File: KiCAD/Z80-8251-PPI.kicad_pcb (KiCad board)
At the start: 2 copper layers, 99.7 x 74.9 mm, 37 parts, among them J1 SBC8080 BUS, J2 ADDR_JP, J3 IR JP, J4 232C-CON, J5 CON-A, J6 CON-B, J7 SERIAL JP, J8 SP JP, Q1 2SC1815, U1 74LS139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

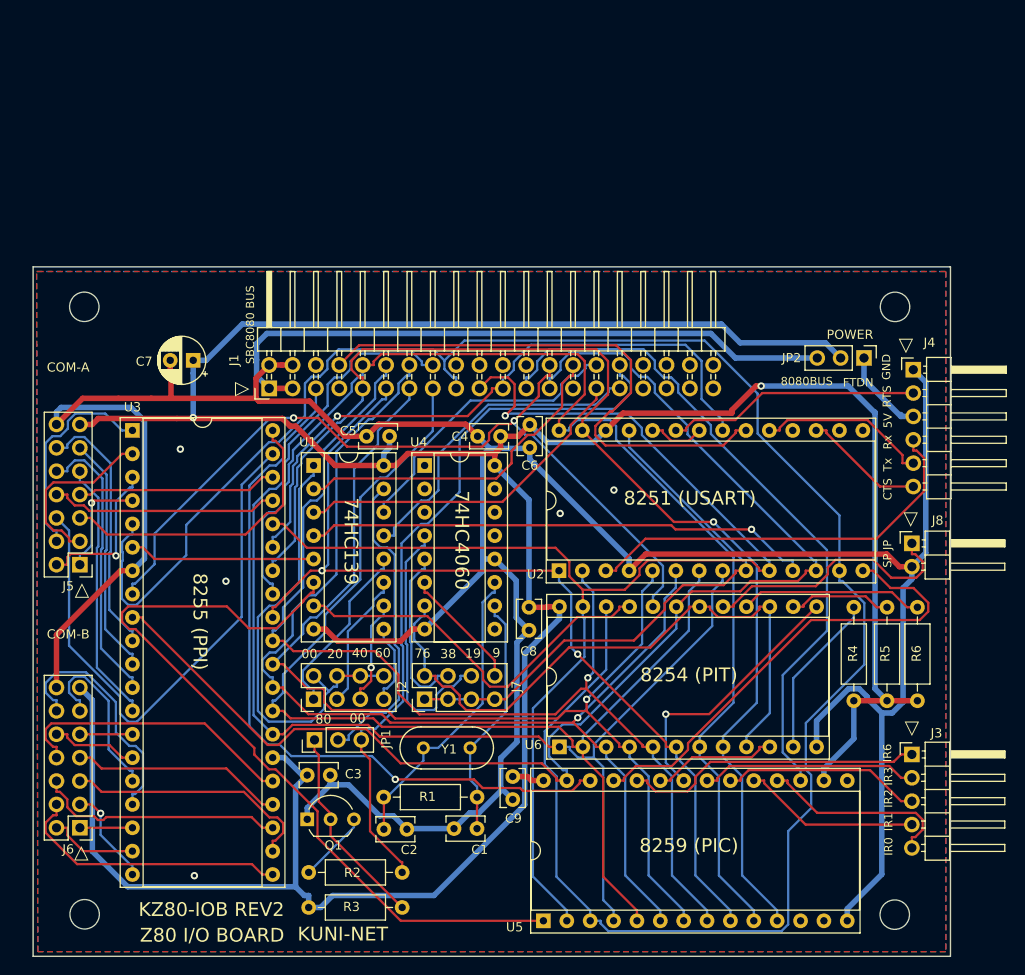
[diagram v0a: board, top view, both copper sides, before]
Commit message: ロジックICで割り込みコントローラ構成を検討 ドラフト版
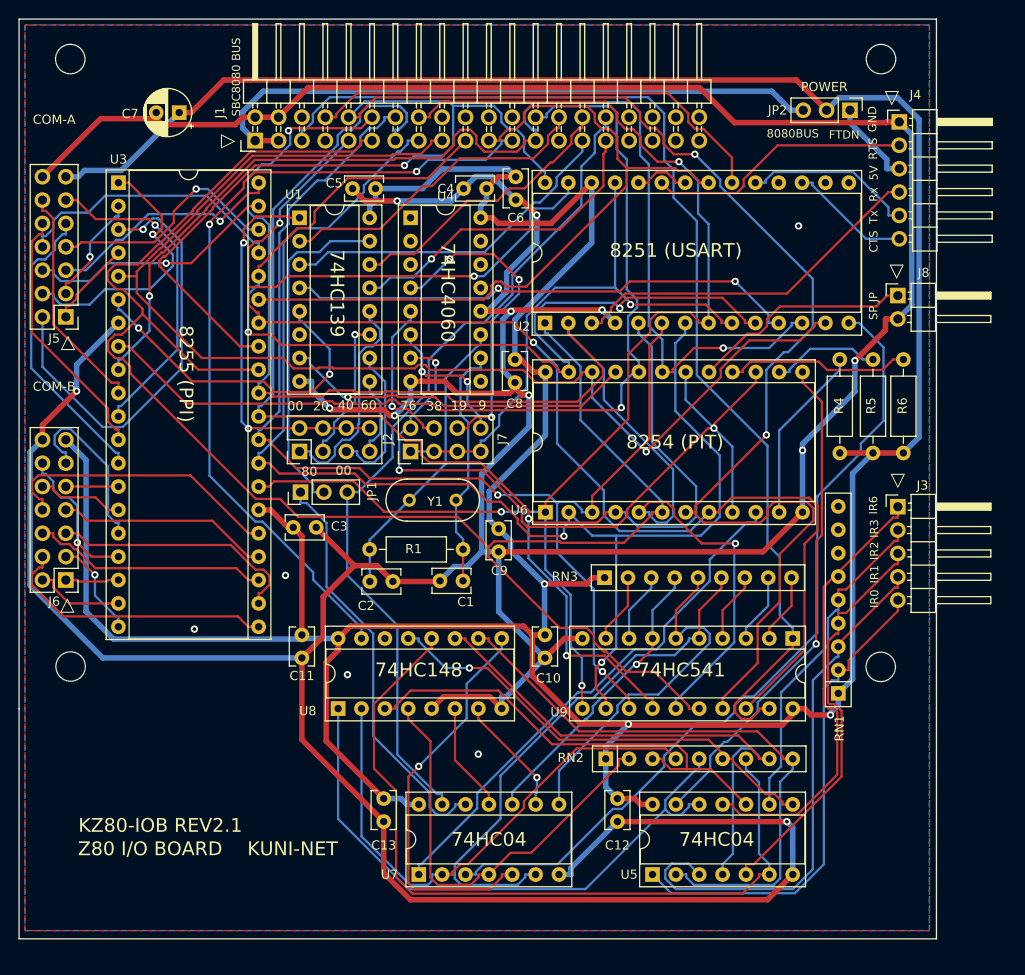
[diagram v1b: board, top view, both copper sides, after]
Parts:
- removed Q1: 2SC1815, Package_TO_SOT_THT:TO-92_Inline_Wide
- removed R2: 100k, Resistor_THT:R_Axial_DIN0207_L6.3mm_D2.5mm_P10.16mm_Horizontal
- removed R3: 1k, Resistor_THT:R_Axial_DIN0207_L6.3mm_D2.5mm_P10.16mm_Horizontal
- added C10: 0.1u, Capacitor_THT:C_Rect_L4.0mm_W2.5mm_P2.50mm, F.Cu at (136.8, 102.9)
- added C11: 0.1u, Capacitor_THT:C_Rect_L4.0mm_W2.5mm_P2.50mm, F.Cu at (110.4, 102.9)
- added C12: 0.1u, Capacitor_THT:C_Rect_L4.0mm_W2.5mm_P2.50mm, F.Cu at (144.7, 120.7)
- added C13: 0.1u, Capacitor_THT:C_Rect_L4.0mm_W2.5mm_P2.50mm, F.Cu at (119.3, 120.7)
- added RN1: 10k, Resistor_THT:R_Array_SIP9, F.Cu at (168.7, 109.2)
- added RN2: 10k, Resistor_THT:R_Array_SIP9, F.Cu at (143.4, 116.3)
- added RN3: 10k, Resistor_THT:R_Array_SIP9, F.Cu at (143.3, 96.6)
- added U7: 74HC04, Package_DIP:DIP-14_W7.62mm_Socket, F.Cu at (123.1, 128.9)
- added U8: 74HC148, Package_DIP:DIP-16_W7.62mm_Socket, F.Cu at (114.3, 110.9)
- added U9: 74HC541, Package_DIP:DIP-20_W7.62mm_Socket, F.Cu at (163.7, 103.3)
- U4: footprint Housings_DIP:DIP-16_W7.62mm_Socket -> Package_DIP:DIP-16_W7.62mm_Socket
- U5: value 8259 -> 74HC04; footprint Package_DIP:DIP-28_W15.24mm_Socket -> Package_DIP:DIP-14_W7.62mm_Socket
- moved C1 27.0 mm to (127.9, 97.0)
- moved C3 27.0 mm to (109.4, 91.2)
- moved C6 27.0 mm to (133.6, 53.1)
- moved C7 27.0 mm to (97.0, 46.1)
- moved J2 27.0 mm to (110.1, 82.9)
- moved J3 27.0 mm to (175.1, 88.9)
- moved J6 27.0 mm to (84.7, 96.9)
- moved J7 27.0 mm to (122.2, 82.9)
- moved J8 27.0 mm to (175.1, 66.0)
- moved JP1 27.0 mm to (110.2, 87.4)
- moved MH2 27.0 mm to (173.3, 40.3)
- moved R1 27.0 mm to (117.7, 93.6)
- moved R4 27.0 mm to (168.8, 83.1)
- moved R5 27.0 mm to (172.4, 83.1)
- moved R6 27.0 mm to (175.7, 83.1)
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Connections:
- U1 pad 6: 8259-CS -> Net-(U1-Pad6)
- U5 pad 1: 8259-CS -> /IR0
- U5 pad 10: D1 -> Net-(RN2-Pad3)
- U5 pad 11: D0 -> /IR6
- U5 pad 13: Net-(U5-Pad13) -> 8254-2
- U5 pad 14: GND -> VCC
- U5 pad 2: ~IOW -> Net-(RN2-Pad9)
- U5 pad 3: ~IOR -> /IR1
- U5 pad 4: D7 -> Net-(RN2-Pad8)
- U5 pad 5: D6 -> /IR2
- U5 pad 6: D5 -> Net-(RN2-Pad7)
- U5 pad 7: D4 -> GND
- U5 pad 8: D3 -> Net-(RN2-Pad6)
- U5 pad 9: D2 -> /IR3
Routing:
- net GND: track 334.3 -> 538.4 mm, vias 5 -> 16
- net ~IOR: track 229.8 -> 135.3 mm, vias 0 -> 1
- net D2: track 103.3 -> 191.4 mm, vias 2 -> 0
- net 8259-CS: track 87.2 -> 0.00 mm
- net Net-(RN2-Pad7): track 0.00 -> 85.7 mm
- net D1: track 134.6 -> 218.4 mm, vias 0 -> 3
- net VCC: track 368.0 -> 450.1 mm, vias 2 -> 3
- net Net-(RN2-Pad5): track 0.00 -> 66.1 mm
- net Net-(RN2-Pad9): track 0.00 -> 65.7 mm
- net Net-(RN3-Pad6): track 0.00 -> 58.5 mm
- net Net-(RN2-Pad8): track 0.00 -> 58.1 mm
- net Net-(RN2-Pad4): track 0.00 -> 57.9 mm
- net Net-(RN2-Pad3): track 0.00 -> 50.6 mm
- net Net-(RN2-Pad6): track 0.00 -> 50.3 mm, vias 0 -> 1
- net Net-(RN2-Pad2): track 0.00 -> 47.5 mm
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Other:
- board size 99.7 x 74.9 mm -> 99.7 x 99.9 mm
- board text added: "74HC04"
- board text added: "74HC148"
- board text added: "74HC541"
- board text added: "KZ80-IOB REV2.1"
- board text removed: "8259 (PIC)"
- board text removed: "KZ80-IOB REV2"
